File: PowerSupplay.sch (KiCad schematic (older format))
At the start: 22 parts, among them J13 Jack-DC, J16 Conn_01x03, U4 AP1117-33, U5 MC34063, U7 78M09

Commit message: add I2S_CLKIN_MCU
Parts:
- removed C25: 330uF, Capacitors_ThroughHole:CP_Radial_D10.0mm_P5.00mm, symbol CP_Small
- removed L1: 280uH, Choke_Axial_ThroughHole:Choke_Horizontal_RM10mm, symbol L_Small
- removed U4: AP1117-33, TO_SOT_Packages_SMD:SOT-223, symbol AP1117-33
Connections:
- wire segments 58 -> 54
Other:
- moved on the sheet: C26
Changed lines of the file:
@@
 $Descr A4 11693 8268
 encoding utf-8
-Sheet 5 6
+Sheet 5 5
 Title ""
 Date ""
@@
 Connection ~ 2100 2400
 $Comp
-L GND #PWR68
+L GND #PWR055
 U 1 1 5DD9A087
 P 4600 1900
-F 0 "#PWR68" H 4600 1650 50  0001 C CNN
+F 0 "#PWR055" H 4600 1650 50  0001 C CNN
 F 1 "GND" H 4600 1750 50  0001 C CNN
 F 2 "" H 4600 1900 50  0001 C CNN
@@
 Connection ~ 3250 2400
 $Comp
-L GND #PWR64
+L GND #PWR056
 U 1 1 5DD9A371
 P 3600 2250
-F 0 "#PWR64" H 3600 2000 50  0001 C CNN
+F 0 "#PWR056" H 3600 2000 50  0001 C CNN
 F 1 "GND" H 3600 2100 50  0001 C CNN
 F 2 "" H 3600 2250 50  0001 C CNN
@@
 $EndComp
 $Comp
-L GND #PWR62
+L GND #PWR057
 U 1 1 5DD9A42B
 P 3400 2150
-F 0 "#PWR62" H 3400 1900 50  0001 C CNN
+F 0 "#PWR057" H 3400 1900 50  0001 C CNN
 F 1 "GND" H 3400 2000 50  0001 C CNN
 F 2 "" H 3400 2150 50  0001 C CNN
@@
 Connection ~ 2150 1350
 $Comp
-L +12V #PWR52
+L +12V #PWR058
 U 1 1 5DD9A4E4
 P 1250 2000
-F 0 "#PWR52" H 1250 1850 50  0001 C CNN
+F 0 "#PWR058" H 1250 1850 50  0001 C CNN
 F 1 "+12V" V 1250 2250 50  0000 C CNN
 F 2 "" H 1250 2000 50  0001 C CNN
@@
 Connection ~ 4150 2400
 $Comp
-L +12V #PWR59
+L +12V #PWR059
 U 1 1 5DD9C169
 P 2700 3250
-F 0 "#PWR59" H 2700 3100 50  0001 C CNN
+F 0 "#PWR059" H 2700 3100 50  0001 C CNN
 F 1 "+12V" V 2700 3500 50  0000 C CNN
 F 2 "" H 2700 3250 50  0001 C CNN
@@
 $EndComp
 $Comp
-L +9V #PWR66
+L +9V #PWR060
 U 1 1 5DD9C2C5
 P 4400 2400
-F 0 "#PWR66" H 4400 2250 50  0001 C CNN
+F 0 "#PWR060" H 4400 2250 50  0001 C CNN
 F 1 "+9V" V 4400 2600 50  0000 C CNN
 F 2 "" H 4400 2400 50  0001 C CNN
@@
 $EndComp
 $Comp
-L +9V #PWR70
+L +9V #PWR061
 U 1 1 5DD9C3E9
 P 5200 3250
-F 0 "#PWR70" H 5200 3100 50  0001 C CNN
+F 0 "#PWR061" H 5200 3100 50  0001 C CNN
 F 1 "+9V" V 5200 3450 50  0000 C CNN
 F 2 "" H 5200 3250 50  0001 C CNN
@@
 $EndComp
 $Comp
-L GND #PWR60
+L GND #PWR062
 U 1 1 5DD9C454
 P 3000 3550
-F 0 "#PWR60" H 3000 3300 50  0001 C CNN
+F 0 "#PWR062" H 3000 3300 50  0001 C CNN
 F 1 "GND" H 3000 3400 50  0001 C CNN
 F 2 "" H 3000 3550 50  0001 C CNN
@@
 $EndComp
 $Comp
-L GND #PWR56
+L GND #PWR063
 U 1 1 5DD9C54A
 P 2100 2650
-F 0 "#PWR56" H 2100 2400 50  0001 C CNN
+F 0 "#PWR063" H 2100 2400 50  0001 C CNN
 F 1 "GND" H 2100 2500 50  0001 C CNN
 F 2 "" H 2100 2650 50  0001 C CNN
@@
 	3300 4450 4250 4450
 Wire Wire Line
-	2700 4950 5850 4950
-Wire Wire Line
 	2500 4950 2050 4950
 Connection ~ 2050 4950
 $Comp
-L GND #PWR67
+L GND #PWR064
 U 1 1 5DD9C919
 P 4550 4450
-F 0 "#PWR67" H 4550 4200 50  0001 C CNN
+F 0 "#PWR064" H 4550 4200 50  0001 C CNN
 F 1 "GND" H 4550 4300 50  0001 C CNN
 F 2 "" H 4550 4450 50  0001 C CNN
@@
 	3550 4550 3550 4600
 $Comp
-L GND #PWR63
+L GND #PWR065
 U 1 1 5DD9C936
 P 3550 4800
-F 0 "#PWR63" H 3550 4550 50  0001 C CNN
+F 0 "#PWR065" H 3550 4550 50  0001 C CNN
 F 1 "GND" H 3550 4650 50  0001 C CNN
 F 2 "" H 3550 4800 50  0001 C CNN
@@
 $EndComp
 $Comp
-L GND #PWR61
+L GND #PWR066
 U 1 1 5DD9C93C
 P 3350 4700
-F 0 "#PWR61" H 3350 4450 50  0001 C CNN
+F 0 "#PWR066" H 3350 4450 50  0001 C CNN
 F 1 "GND" H 3350 4550 50  0001 C CNN
 F 2 "" H 3350 4700 50  0001 C CNN
@@
 Connection ~ 4100 4450
 Wire Wire Line
-	4100 4800 4100 4950
+	4100 4950 4100 4800
 Connection ~ 4100 4950
 $Comp
-L GND #PWR58
-U 1 1 5DD9C97A
-P 2550 5900
-F 0 "#PWR58" H 2550 5650 50  0001 C CNN
-F 1 "GND" H 2550 5750 50  0001 C CNN
-F 2 "" H 2550 5900 50  0001 C CNN
-F 3 "" H 2550 5900 50  0001 C CNN
-	1    2550 5900
-	1    0    0    -1
-$EndComp
-$Comp
-L GND #PWR65
+L GND #PWR067
 U 1 1 5DD9C980
 P 3850 5200
-F 0 "#PWR65" H 3850 4950 50  0001 C CNN
+F 0 "#PWR067" H 3850 4950 50  0001 C CNN
 F 1 "GND" H 3850 5050 50  0001 C CNN
 F 2 "" H 3850 5200 50  0001 C CNN
@@
 $EndComp
 $Comp
-L GND #PWR55
+L GND #PWR068
 U 1 1 5DD9C98C
 P 2050 5200
-F 0 "#PWR55" H 2050 4950 50  0001 C CNN
+F 0 "#PWR068" H 2050 4950 50  0001 C CNN
 F 1 "GND" H 2050 5050 50  0001 C CNN
 F 2 "" H 2050 5200 50  0001 C CNN
@@
 $EndComp
 $Comp
-L GND #PWR54
+L GND #PWR069
 U 1 1 5DD9C992
 P 1600 4850
-F 0 "#PWR54" H 1600 4600 50  0001 C CNN
+F 0 "#PWR069" H 1600 4600 50  0001 C CNN
 F 1 "GND" H 1600 4700 50  0001 C CNN
 F 2 "" H 1600 4850 50  0001 C CNN
@@
 $EndComp
 $Comp
-L L_Small L1
-U 1 1 5DDE4A61
-P 5950 4950
-F 0 "L1" V 6150 5000 50  0000 L CNN
-F 1 "280uH" V 6050 4850 50  0000 L CNN
-F 2 "Choke_Axial_ThroughHole:Choke_Horizontal_RM10mm" H 5950 4950 50  0001 C CNN
-F 3 "" H 5950 4950 50  0001 C CNN
-	1    5950 4950
-	0    -1   -1   0
-$EndComp
-$Comp
-L +3V3 #PWR75
+L +3V3 #PWR070
 U 1 1 5DDE50CB
-P 6800 4950
-F 0 "#PWR75" H 6800 4800 50  0001 C CNN
-F 1 "+3V3" V 6800 5200 50  0000 C CNN
-F 2 "" H 6800 4950 50  0001 C CNN
-F 3 "" H 6800 4950 50  0001 C CNN
-	1    6800 4950
+P 4650 4950
+F 0 "#PWR070" H 4650 4800 50  0001 C CNN
+F 1 "+3V3" V 4650 5200 50  0000 C CNN
+F 2 "" H 4650 4950 50  0001 C CNN
+F 3 "" H 4650 4950 50  0001 C CNN
+	1    4650 4950
 	0    1    1    0
 $EndComp
 Wire Wire Line
-	6050 4950 6800 4950
-$Comp
-L CP_Small C25
-U 1 1 5DDE528C
-P 6200 5100
-F 0 "C25" H 6300 5150 50  0000 L CNN
-F 1 "330uF" H 6300 5050 50  0000 L CNN
-F 2 "Capacitors_ThroughHole:CP_Radial_D10.0mm_P5.00mm" H 6200 5100 50  0001 C CNN
-F 3 "" H 6200 5100 50  0001 C CNN
-	1    6200 5100
-	1    0    0    -1
-$EndComp
+	2700 4950 4650 4950
 $Comp
 L C_Small C26
 U 1 1 5DDE5430
-P 6700 5100
-F 0 "C26" H 6800 5150 50  0000 L CNN
-F 1 "100nF" H 6800 5050 50  0000 L CNN
-F 2 "UI:C_1206_0603" H 6700 5100 50  0001 C CNN
-F 3 "" H 6700 5100 50  0001 C CNN
-	1    6700 5100
-	1    0    0    -1
-$EndComp
-$Comp
-L GND #PWR71
-U 1 1 5DDE5565
-P 6200 5200
-F 0 "#PWR71" H 6200 4950 50  0001 C CNN
-F 1 "GND" H 6200 5050 50  0001 C CNN
-F 2 "" H 6200 5200 50  0001 C CNN
-F 3 "" H 6200 5200 50  0001 C CNN
-	1    6200 5200
-	1    0    0    -1
-$EndComp
-$Comp
-L GND #PWR74
+P 4450 5100
+F 0 "C26" H 4550 5150 50  0000 L CNN
+F 1 "100nF" H 4550 5050 50  0000 L CNN
+F 2 "UI:C_1206_0603" H 4450 5100 50  0001 C CNN
+F 3 "" H 4450 5100 50  0001 C CNN
+	1    4450 5100
+	1    0    0    -1
+$EndComp
+$Comp
+L GND #PWR071
 U 1 1 5DDE5612
-P 6700 5200
-F 0 "#PWR74" H 6700 4950 50  0001 C CNN
-F 1 "GND" H 6700 5050 50  0001 C CNN
-F 2 "" H 6700 5200 50  0001 C CNN
-F 3 "" H 6700 5200 50  0001 C CNN
-	1    6700 5200
-	1    0    0    -1
-$EndComp
-Wire Wire Line
-	6200 5000 6200 4950
-Connection ~ 6200 4950
-Wire Wire Line
-	6700 5000 6700 4950
-Connection ~ 6700 4950
+P 4450 5200
+F 0 "#PWR071" H 4450 4950 50  0001 C CNN
+F 1 "GND" H 4450 5050 50  0001 C CNN
+F 2 "" H 4450 5200 50  0001 C CNN
+F 3 "" H 4450 5200 50  0001 C CNN
+	1    4450 5200
+	1    0    0    -1
+$EndComp
 $Comp
 L MC34063 U5
@@
 $EndComp
 $Comp
-L AP1117-33 U4
-U 1 1 5DDFE5A2
-P 2550 5600
-F 0 "U4" H 2700 5800 50  0000 C CNN
-F 1 "AP1117-33" H 2550 5725 50  0000 L CNN
-F 2 "TO_SOT_Packages_SMD:SOT-223" H 2550 5800 50  0001 C CNN
-F 3 "" H 2650 5350 50  0001 C CNN
-	1    2550 5600
-	1    0    0    -1
-$EndComp
-$Comp
-L +9V #PWR57
-U 1 1 5DE21DEE
-P 2250 5600
-F 0 "#PWR57" H 2250 5450 50  0001 C CNN
-F 1 "+9V" V 2250 5800 50  0000 C CNN
-F 2 "" H 2250 5600 50  0001 C CNN
-F 3 "" H 2250 5600 50  0001 C CNN
-	1    2250 5600
-	0    -1   -1   0
-$EndComp
-$Comp
-L +12V #PWR53
+L +12V #PWR072
 U 1 1 5E97FA32
 P 1400 4550
-F 0 "#PWR53" H 1400 4400 50  0001 C CNN
+F 0 "#PWR072" H 1400 4400 50  0001 C CNN
 F 1 "+12V" V 1400 4800 50  0000 C CNN
 F 2 "" H 1400 4550 50  0001 C CNN
@@
 	3850 5000 3850 4950
 Connection ~ 3850 4950
-Wire Wire Line
-	4950 4950 4950 5600
-Connection ~ 4950 4950
 $Comp
 L Jack-DC J13
@@
 $EndComp
 $Comp
-L +12V #PWR73
+L +12V #PWR073
 U 1 1 5E994C0D
 P 6500 2100
-F 0 "#PWR73" H 6500 1950 50  0001 C CNN
+F 0 "#PWR073" H 6500 1950 50  0001 C CNN
 F 1 "+12V" V 6500 2350 50  0000 C CNN
 F 2 "" H 6500 2100 50  0001 C CNN
@@
 	6250 2100 6500 2100
 $Comp
-L GND #PWR72
+L GND #PWR074
 U 1 1 5E994E36
 P 6300 2350
-F 0 "#PWR72" H 6300 2100 50  0001 C CNN
+F 0 "#PWR074" H 6300 2100 50  0001 C CNN
 F 1 "GND" H 6300 2200 50  0001 C CNN
 F 2 "" H 6300 2350 50  0001 C CNN
@@
 Connection ~ 6300 2300
 Wire Wire Line
-	2850 5600 5300 5600
-Connection ~ 4950 5600
-Wire Wire Line
 	3300 3250 5200 3250
 Wire Wire Line
@@
 Connection ~ 5100 3250
 $Comp
-L GND #PWR69
+L GND #PWR075
 U 1 1 5E9B2413
 P 5150 5850
-F 0 "#PWR69" H 5150 5600 50  0001 C CNN
+F 0 "#PWR075" H 5150 5600 50  0001 C CNN
 F 1 "GND" H 5150 5700 50  0001 C CNN
 F 2 "" H 5150 5850 50  0001 C CNN
@@
 	1    0    0    -1
 $EndComp
+Wire Wire Line
+	4450 5000 4450 4950
+Connection ~ 4450 4950
 $EndSCHEMATC

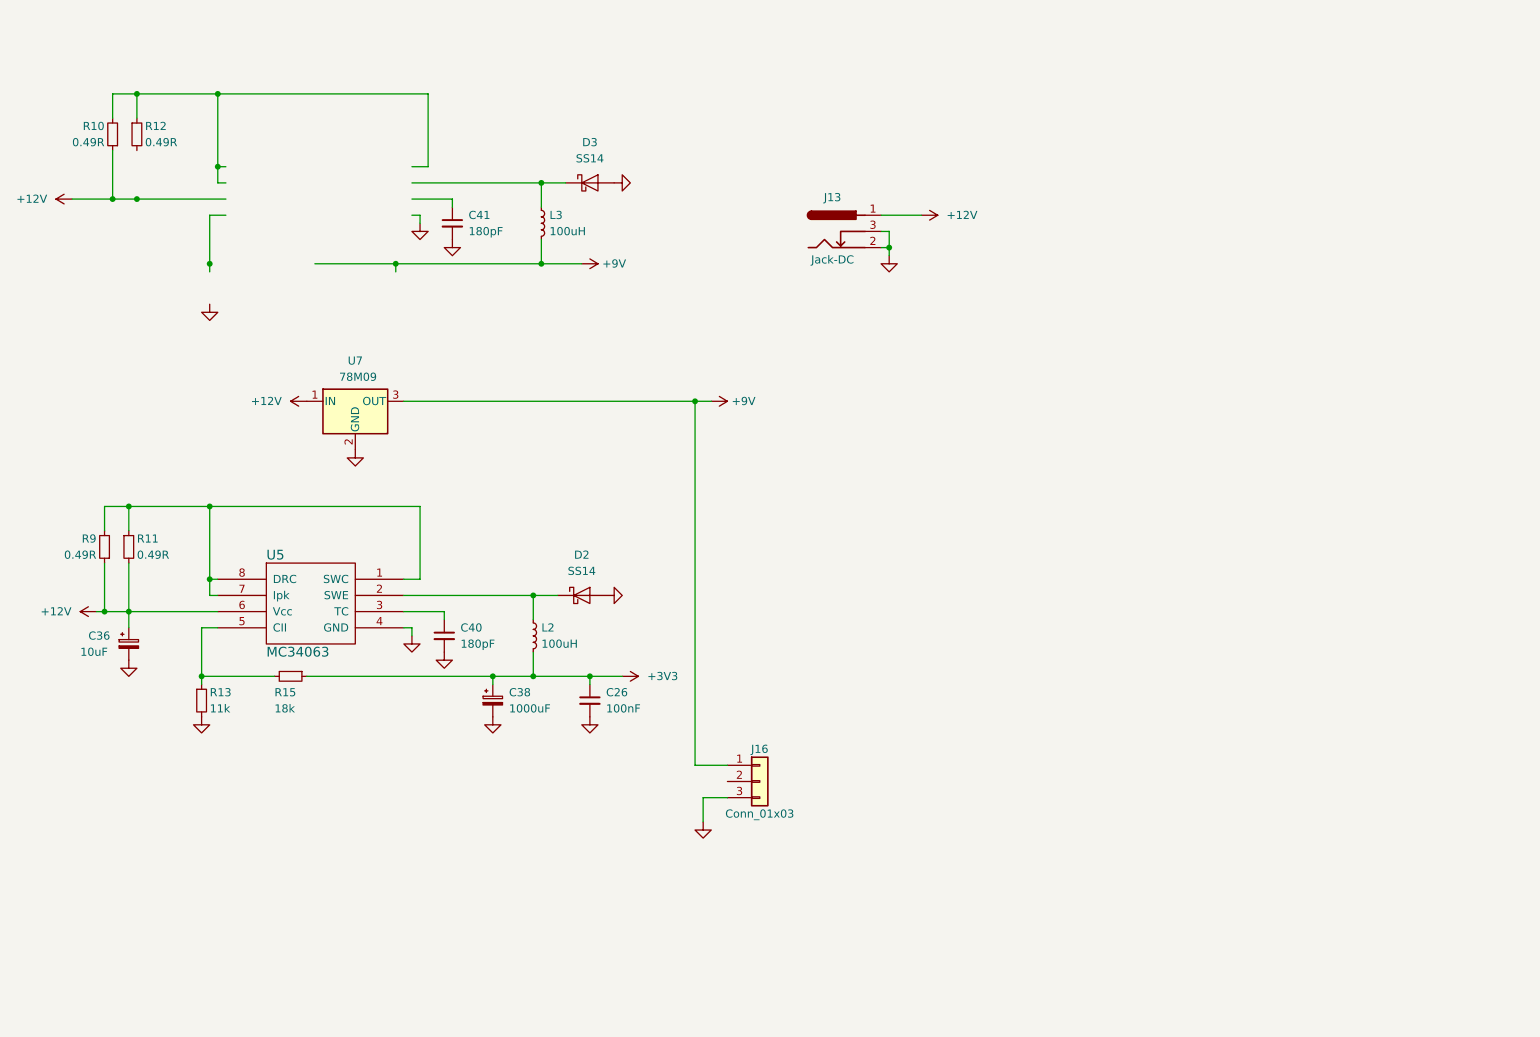
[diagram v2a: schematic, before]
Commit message: PCB almost ready, needs some GND vias
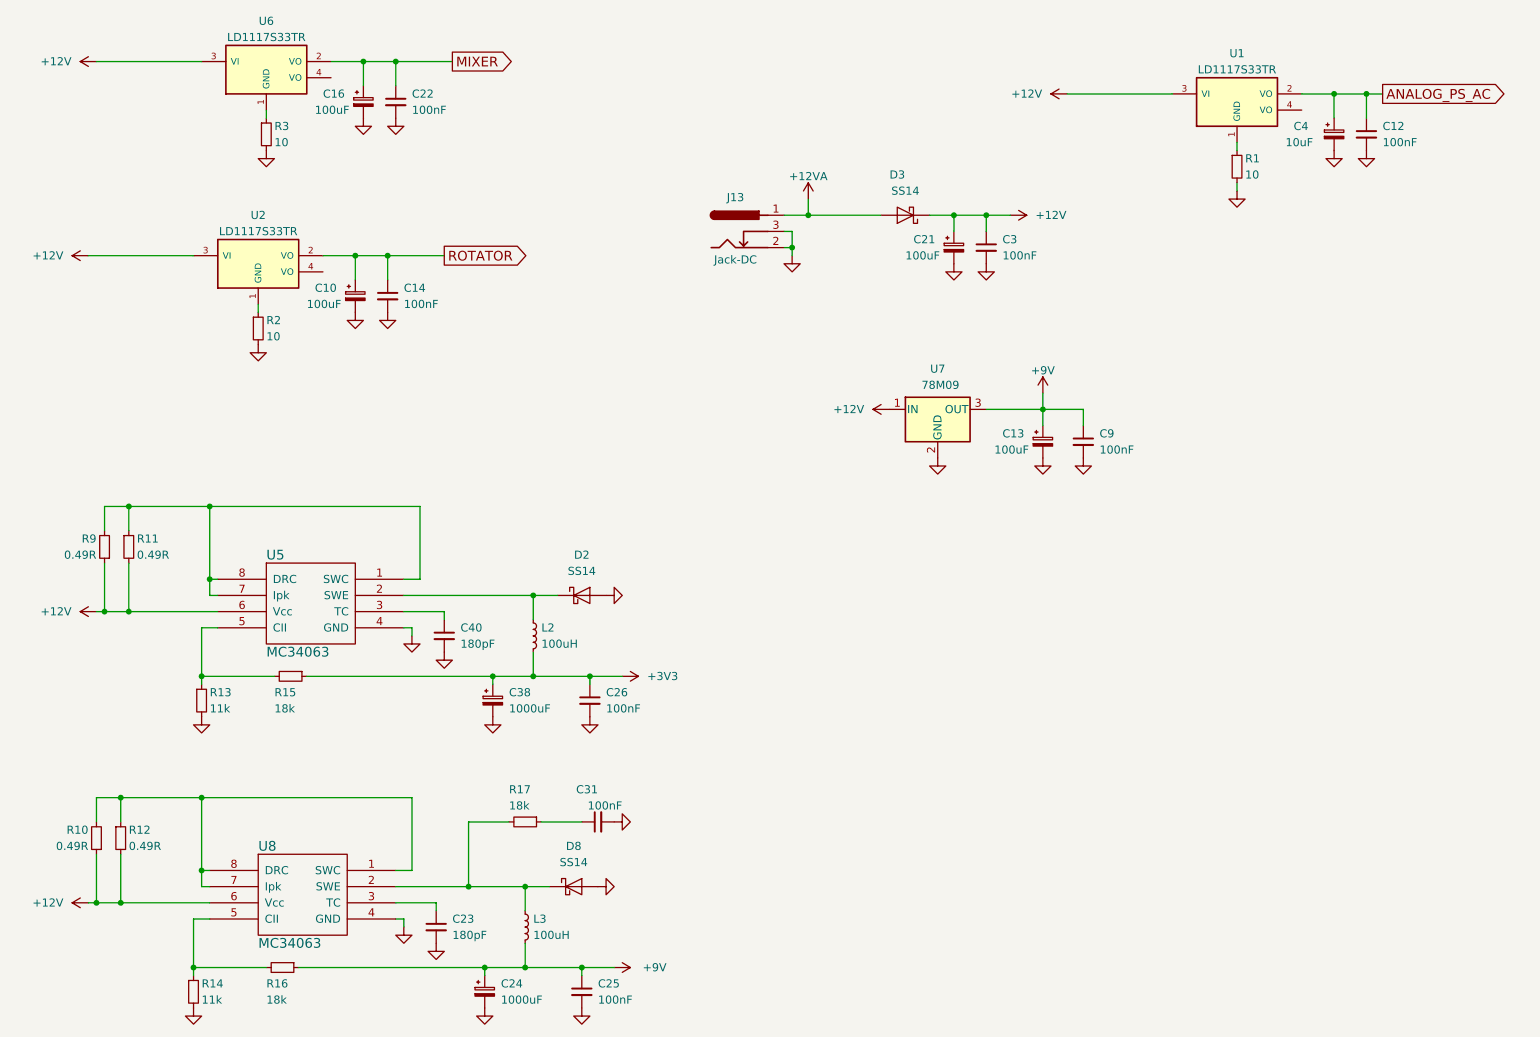
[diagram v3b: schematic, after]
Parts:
- removed C36: 10uF, Capacitors_THT:CP_Radial_D6.3mm_P2.50mm, symbol CP_Small
- removed C41: 180pF, UI:C_1206_0603, symbol C_Small
- removed J16: Conn_01x03, symbol Conn_01x03
- added C10, C13, C16, C21: 100uF, Capacitors_THT:CP_Radial_D6.3mm_P2.50mm, symbol CP_Small
- added C12, C14, C22, C25, C3, C31, C9: 100nF, UI:C_1206_0603, symbol C_Small
- added C23: 180pF, UI:C_1206_0603, symbol C_Small
- added C24: 1000uF, Capacitors_THT:CP_Radial_D10.0mm_P5.00mm, symbol CP_Small
- added C4: 10uF, Capacitors_THT:CP_Radial_D5.0mm_P2.00mm, symbol CP_Small
- added D8: SS14, Diodes_SMD:D_SMA_Handsoldering, symbol D_Schottky
- added R1, R2, R3: 10, UI:R_1206_0603, symbol R_Small
- added R14: 11k, UI:R_1206_0603, symbol R_Small
- added R16, R17: 18k, UI:R_1206_0603, symbol R_Small
- added U1, U2, U6: LD1117S33TR, TO_SOT_Packages_SMD:SOT-223, symbol LD1117S33TR
- added U8: MC34063, UI:SOIC-8_3.9x4.9mm_Pitch1.27mm, symbol MC34063
- C38: footprint Capacitors_ThroughHole:CP_Radial_D10.0mm_P5.00mm -> Capacitors_THT:CP_Radial_D10.0mm_P5.00mm
- L2, L3: footprint Choke_Toroid_ThroughHole:Choke_Toroid_5x10mm_Vertical -> Choke_Toroid_ThroughHole:Choke_Toroid_6,5x13mm_Vertical
- R10, R11, R12, R9: footprint Resistors_ThroughHole:R_Axial_DIN0207_L6.3mm_D2.5mm_P10.16mm_Horizontal -> Resistors_THT:R_Axial_DIN0204_L3.6mm_D1.6mm_P7.62mm_Horizontal
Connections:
- net labels added: +12VA, ANALOG_PS_AC, MIXER, ROTATOR
- wire segments 54 -> 78
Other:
- moved on the sheet: J13, U7
